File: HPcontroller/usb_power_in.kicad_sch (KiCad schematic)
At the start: 24 parts, among them J2 UJ20-C-H-G-SMT-1-P16-TR, U5 AP33771C

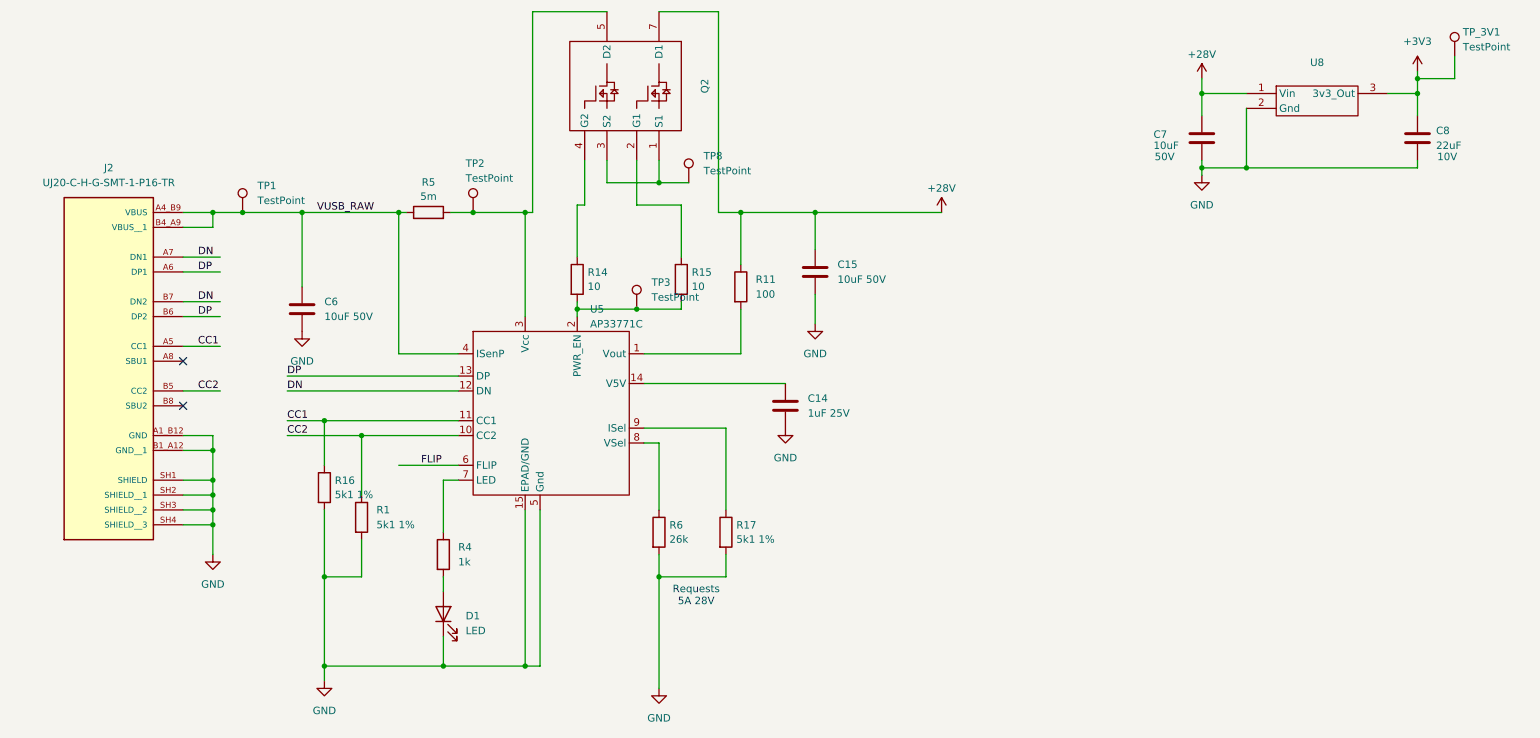
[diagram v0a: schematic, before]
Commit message: released rev c - op amp swap not fixed!
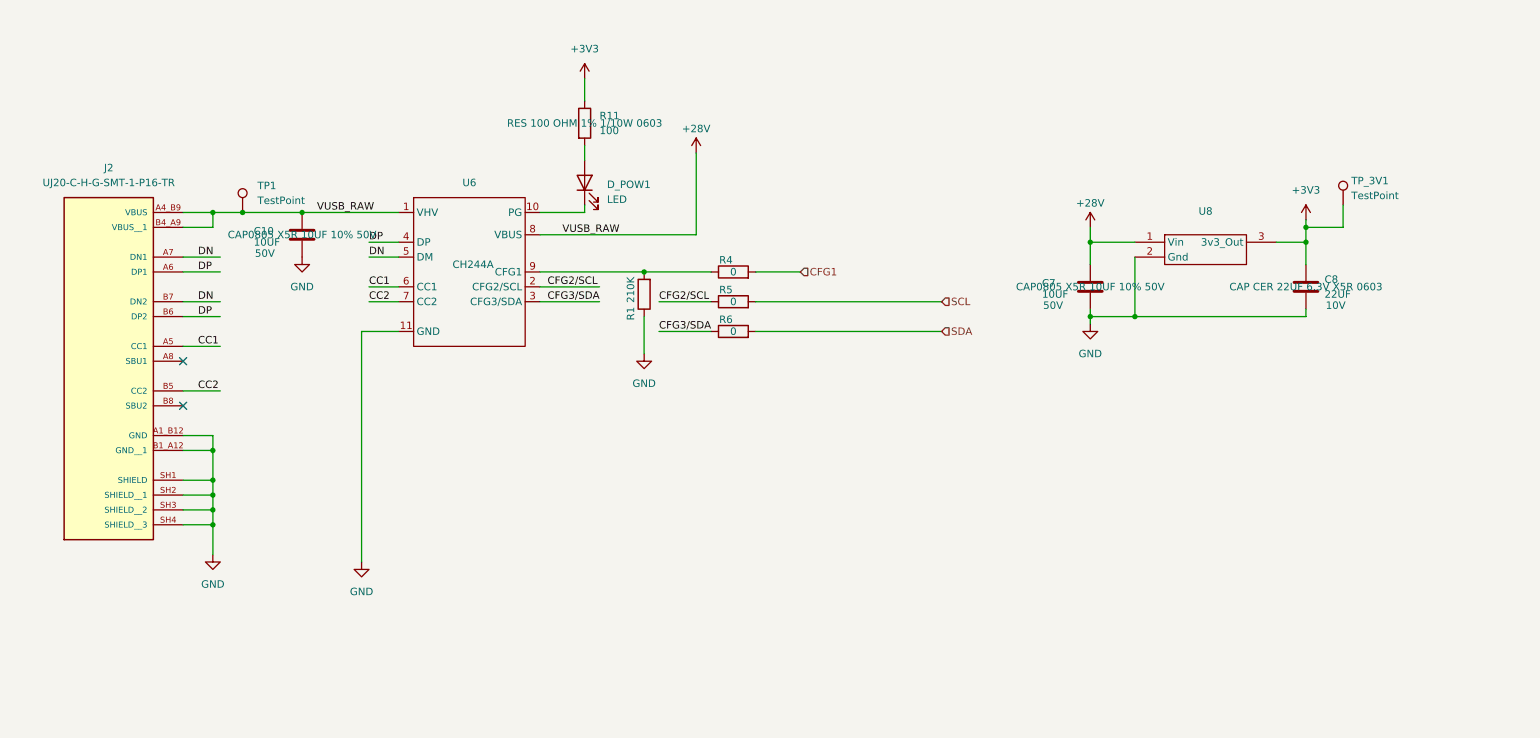
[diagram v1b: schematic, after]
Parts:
- removed C14: 1uF 25V, Capacitor_SMD:C_0402_1005Metric, symbol Device:C
- removed C15, C6: 10uF 50V, Capacitor_SMD:C_1206_3216Metric_Pad1.33x1.80mm_HandSolder, symbol Device:C
- removed D1: LED, LED_SMD:LED_0603_1608Metric_Pad1.05x0.95mm_HandSolder, symbol Device:LED
- removed Q2: ~, hotplate_Library:LFPAK56D, symbol Hotplate_Library:BUK9K25-40RAX
- removed R14, R15: 10, Resistor_SMD:R_0402_1005Metric, symbol Device:R
- removed R16, R17: 5k1 1%, Resistor_SMD:R_0402_1005Metric, symbol Device:R
- removed TP2, TP3, TP8: TestPoint, TestPoint:TestPoint_Pad_D1.5mm, symbol Connector:TestPoint
- removed U5: AP33771C, Package_DFN_QFN:DFN-14-1EP_3x3mm_P0.4mm_EP1.78x2.35mm, symbol C_buck_syms:AP33771C
- added C10: 10UF, Capacitor_SMD:C_0805_2012Metric, symbol Device:C
- added D_POW1: LED, LED_SMD:LED_0603_1608Metric_Pad1.05x0.95mm_HandSolder, symbol Device:LED
- added U6: CH244A, Package_SO:SSOP-10-1EP_3.9x4.9mm_P1mm_EP2.1x3.3mm, symbol Hotplate_Library:CH224A
- C7: value 10uF -> 10UF; MPN GRM21BR61H106KE43L -> GMC21X5R106K50NT; Manufacturer (none) -> Cal-Chip Electronics, Inc.; Package (none) -> 0805; Supplier (none) -> DigiKey; Supplier_PN (none) -> 4713-GMC21X5R106K50NTCT-ND
- C8: value 22uF -> 22UF; MPN CL10A226MP8NUNE -> CL10A226MQ8NRNE; Manufacturer (none) -> Samsung Electro-Mechanics; Package (none) -> 0603; Supplier (none) -> DigiKey; Supplier_PN (none) -> 1276-2868-1-ND
- J2: Manufacturer (none) -> Same Sky (Formerly CUI Devices); Supplier (none) -> DigiKey; Supplier_PN (none) -> 2223-UJ20-C-H-G-SMT-1-P16-TRCT-ND
- R1: value 5k1 1% -> 210K; footprint Resistor_SMD:R_0402_1005Metric -> Resistor_SMD:R_0603_1608Metric; MPN RC0402FR-135K1L -> RMCF0603FT210K; Manufacturer (none) -> Stackpole Electronics Inc; Package (none) -> 0603; Supplier (none) -> DigiKey; Supplier_PN (none) -> RMCF0603FT210KCT-ND
- R11: footprint Resistor_SMD:R_0402_1005Metric -> Resistor_SMD:R_0603_1608Metric; Digikey PN (none) -> A130128CT-ND; MPN RC0402FR-07100RL -> RMCF0603FT100R; Manufacturer (none) -> Stackpole Electronics Inc; Package (none) -> 0603; Supplier (none) -> DigiKey; Supplier_PN (none) -> RMCF0603FT100RCT-ND
- R4: value 1k -> 0; footprint Resistor_SMD:R_0402_1005Metric -> Resistor_SMD:R_0805_2012Metric_Pad1.20x1.40mm_HandSolder; MPN RC0402FR-071KL -> RMCF0805ZT0R00; Manufacturer (none) -> Stackpole Electronics Inc; Package (none) -> 0805; Supplier (none) -> DigiKey; Supplier_PN (none) -> RMCF0805ZT0R00CT-ND
- R5: value 5m -> 0; footprint Resistor_SMD:R_0603_1608Metric -> Resistor_SMD:R_0805_2012Metric_Pad1.20x1.40mm_HandSolder; MPN PA0603FRE470R005L -> RMCF0805ZT0R00; Manufacturer (none) -> Stackpole Electronics Inc; Package (none) -> 0805; Supplier (none) -> DigiKey; Supplier_PN (none) -> RMCF0805ZT0R00CT-ND
- R6: value 26k -> 0; footprint Resistor_SMD:R_0603_1608Metric -> Resistor_SMD:R_0805_2012Metric_Pad1.20x1.40mm_HandSolder; MPN RC0603FR-0726K1L -> RMCF0805ZT0R00; Manufacturer (none) -> Stackpole Electronics Inc; Package (none) -> 0805; Supplier (none) -> DigiKey; Supplier_PN (none) -> RMCF0805ZT0R00CT-ND; Tol 1% -> (none)
- U8: value ~ -> (none); Manufacturer (none) -> Diwell Electronics; Package (none) -> -; Supplier (none) -> DigiKey; Supplier_PN (none) -> 4369-D78B33-0.5-ND
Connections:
- net +28V: now also J2.A4_B9 (VBUS), J2.B4_A9 (VBUS__1), TP1.1, C10.1, U6.1 (VHV), U6.8 (VBUS); no longer R11.1
- net +3V3: now also R11.1
- net CC1: now also U6.6 (CC1)
- net CC2: now also U6.7 (CC2); no longer R1.1
- net DN: now also U6.5 (DM)
- net DP: now also U6.4 (DP)
- net GND: now also R1.1, C10.2, U6.11 (GND); no longer R1.2, R6.2
- net SCL: now reaches R5.2
- net at R11.2: now also D_POW1.2 (A)
- net at R4.1: now also R1.2, U6.9 (CFG1)
- net CFG1: now reaches R4.2
- net CFG3/SDA: now reaches R6.1
- net CFG3/SDA: now also U6.3 (CFG3/SDA)
- removed net VUSB_RAW: J2.A4_B9 (VBUS), J2.B4_A9 (VBUS__1), R5.1, TP1.1
- new net: D_POW1.1 (K), U6.10 (PG)
- new net CFG2/SCL: R5.1, U6.2 (CFG2/SCL)
- new net SDA: R6.2
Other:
- note removed: "Requests 5A 28V"
- moved on the sheet: C7, C8, TP_3V1, U8
